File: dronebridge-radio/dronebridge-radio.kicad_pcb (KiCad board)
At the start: 2 copper layers, 20.5 x 28.5 mm, 4 parts, among them J1 Conn_01x06_Pin

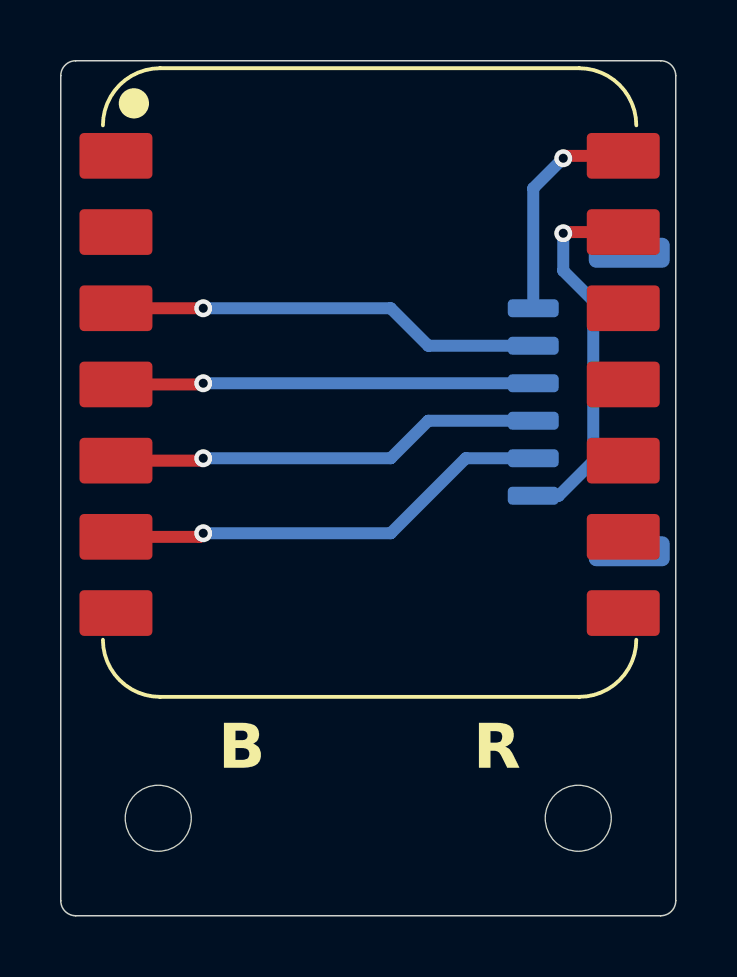
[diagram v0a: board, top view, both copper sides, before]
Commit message: fix swap reset and boot labels on the board
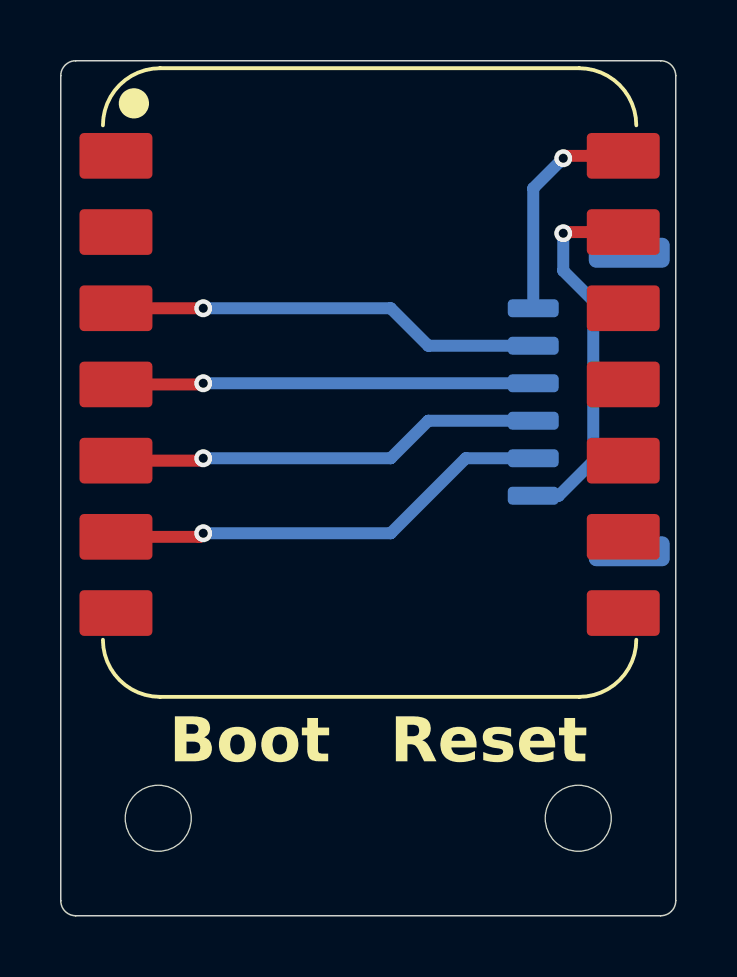
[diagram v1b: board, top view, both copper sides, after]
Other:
- board text added: "Boot"
- board text added: "Reset"
- board text removed: "B"
- board text removed: "R"
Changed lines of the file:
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@@
 (kicad_pcb
-	(version 20240108)
+	(version 20241229)
 	(generator "pcbnew")
-	(generator_version "8.0")
+	(generator_version "9.0")
 	(general
 		(thickness 1.6)
@@
 	(layers
 		(0 "F.Cu" signal)
-		(31 "B.Cu" signal)
-		(32 "B.Adhes" user "B.Adhesive")
-		(33 "F.Adhes" user "F.Adhesive")
-		(34 "B.Paste" user)
-		(35 "F.Paste" user)
-		(36 "B.SilkS" user "B.Silkscreen")
-		(37 "F.SilkS" user "F.Silkscreen")
-		(38 "B.Mask" user)
-		(39 "F.Mask" user)
-		(40 "Dwgs.User" user "User.Drawings")
-		(41 "Cmts.User" user "User.Comments")
-		(42 "Eco1.User" user "User.Eco1")
-		(43 "Eco2.User" user "User.Eco2")
-		(44 "Edge.Cuts" user)
-		(45 "Margin" user)
-		(46 "B.CrtYd" user "B.Courtyard")
-		(47 "F.CrtYd" user "F.Courtyard")
-		(48 "B.Fab" user)
-		(49 "F.Fab" user)
-		(50 "User.1" user)
-		(51 "User.2" user)
-		(52 "User.3" user)
-		(53 "User.4" user)
-		(54 "User.5" user)
-		(55 "User.6" user)
-		(56 "User.7" user)
-		(57 "User.8" user)
-		(58 "User.9" user)
+		(2 "B.Cu" signal)
+		(9 "F.Adhes" user "F.Adhesive")
+		(11 "B.Adhes" user "B.Adhesive")
+		(13 "F.Paste" user)
+		(15 "B.Paste" user)
+		(5 "F.SilkS" user "F.Silkscreen")
+		(7 "B.SilkS" user "B.Silkscreen")
+		(1 "F.Mask" user)
+		(3 "B.Mask" user)
+		(17 "Dwgs.User" user "User.Drawings")
+		(19 "Cmts.User" user "User.Comments")
+		(21 "Eco1.User" user "User.Eco1")
+		(23 "Eco2.User" user "User.Eco2")
+		(25 "Edge.Cuts" user)
+		(27 "Margin" user)
+		(31 "F.CrtYd" user "F.Courtyard")
+		(29 "B.CrtYd" user "B.Courtyard")
+		(35 "F.Fab" user)
+		(33 "B.Fab" user)
+		(39 "User.1" user)
+		(41 "User.2" user)
+		(43 "User.3" user)
+		(45 "User.4" user)
+		(47 "User.5" user)
+		(49 "User.6" user)
+		(51 "User.7" user)
+		(53 "User.8" user)
+		(55 "User.9" user)
 	)
 	(setup
@@
 		(pad_to_mask_clearance 0)
 		(allow_soldermask_bridges_in_footprints no)
+		(tenting front back)
 		(pcbplotparams
-			(layerselection 0x00010fc_ffffffff)
-			(plot_on_all_layers_selection 0x0000000_00000000)
+			(layerselection 0x00000000_00000000_55555555_5755f5ff)
+			(plot_on_all_layers_selection 0x00000000_00000000_00000000_00000000)
 			(disableapertmacros no)
 			(usegerberextensions no)
@@
 			(svgprecision 4)
 			(plotframeref no)
-			(viasonmask no)
 			(mode 1)
 			(useauxorigin no)
@@
 			(pdf_front_fp_property_popups yes)
 			(pdf_back_fp_property_popups yes)
+			(pdf_metadata yes)
+			(pdf_single_document no)
 			(dxfpolygonmode yes)
 			(dxfimperialunits yes)
@@
 			(psnegative no)
 			(psa4output no)
-			(plotreference yes)
-			(plotvalue yes)
-			(plotfptext yes)
-			(plotinvisibletext no)
+			(plot_black_and_white yes)
 			(sketchpadsonfab no)
+			(plotpadnumbers no)
+			(hidednponfab no)
+			(sketchdnponfab yes)
+			(crossoutdnponfab yes)
 			(subtractmaskfromsilk no)
 			(outputformat 1)
@@
 			)
 		)
-		(property "Footprint" "XIAO-ESP32C3-footprints:XIAO-ESP32C3-DIP"
-			(at -0.12 0 90)
-			(unlocked yes)
-			(layer "F.Fab")
-			(hide yes)
-			(effects
-				(font
-					(size 1.27 1.27)
-					(thickness 0.15)
-				)
-			)
-		)
 		(property "Datasheet" ""
 			(at -0.12 0 90)
@@
 				(type solid)
 			)
-			(fill solid)
+			(fill yes)
 			(layer "F.SilkS")
 		)
@@
 				(type default)
 			)
-			(fill none)
+			(fill no)
 			(layer "F.CrtYd")
 		)
@@
 				(type default)
 			)
-			(fill none)
+			(fill no)
 			(layer "F.Fab")
 		)
@@
 				(type solid)
 			)
-			(fill solid)
+			(fill yes)
 			(layer "F.Fab")
 		)
@@
 			(thermal_bridge_angle 45)
 		)
+		(embedded_fonts no)
 		(model "${KIPRJMOD}/XIAO-ESP32C3-footprints/3dmodels/AMz3D.3dshapes/Seeed Studio XIAO-ESP32-C3.step"
 			(offset
@@
 			)
 		)
-		(property "Footprint" "MountingHole:MountingHole_2.2mm_M2"
-			(at 0 0 0)
-			(unlocked yes)
-			(layer "F.Fab")
-			(hide yes)
-			(effects
-				(font
-					(size 1.27 1.27)
-					(thickness 0.15)
-				)
-			)
-		)
 		(property "Datasheet" ""
 			(at 0 0 0)
@@
 				(type solid)
 			)
-			(fill none)
+			(fill no)
 			(layer "Cmts.User")
 		)
@@
 				(type solid)
 			)
-			(fill none)
+			(fill no)
 			(layer "F.CrtYd")
 		)
@@
 			(layers "*.Cu" "*.Mask")
 		)
+		(embedded_fonts no)
 	)
 	(footprint "MountingHole:MountingHole_2.2mm_M2"
@@
 			)
 		)
-		(property "Footprint" "MountingHole:MountingHole_2.2mm_M2"
-			(at 0 0 0)
-			(unlocked yes)
-			(layer "F.Fab")
-			(hide yes)
-			(effects
-				(font
-					(size 1.27 1.27)
-					(thickness 0.15)
-				)
-			)
-		)
 		(property "Datasheet" ""
 			(at 0 0 0)
@@
 				(type solid)
 			)
-			(fill none)
+			(fill no)
 			(layer "Cmts.User")
 		)
@@
 				(type solid)
 			)
-			(fill none)
+			(fill no)
 			(layer "F.CrtYd")
 		)
@@
 			(layers "*.Cu" "*.Mask")
 		)
+		(embedded_fonts no)
 	)
 	(footprint "Connector_JST:JST_GH_SM06B-GHS-TB_1x06-1MP_P1.25mm_Horizontal"
@@
 			)
 		)
-		(property "Footprint" "Connector_JST:JST_GH_SM06B-GHS-TB_1x06-1MP_P1.25mm_Horizontal"
-			(at 0 0 90)
-			(unlocked yes)
-			(layer "B.Fab")
-			(hide yes)
-			(effects
-				(font
-					(size 1.27 1.27)
-					(thickness 0.15)
-				)
-				(justify mirror)
-			)
-		)
 		(property "Datasheet" ""
 			(at 0 0 90)
@@
 			(at -3.125 1.85 270)
 			(size 0.6 1.7)
-			(layers "B.Cu" "B.Paste" "B.Mask")
+			(layers "B.Cu" "B.Mask" "B.Paste")
 			(roundrect_rratio 0.25)
 			(net 12 "+5V")
@@
 			(at -1.875 1.85 270)
 			(size 0.6 1.7)
-			(layers "B.Cu" "B.Paste" "B.Mask")
+			(layers "B.Cu" "B.Mask" "B.Paste")
 			(roundrect_rratio 0.25)
 			(net 13 "/RX")
@@
 			(at -0.625 1.85 270)
 			(size 0.6 1.7)
-			(layers "B.Cu" "B.Paste" "B.Mask")
+			(layers "B.Cu" "B.Mask" "B.Paste")
 			(roundrect_rratio 0.25)
 			(net 3 "/TX")
@@
 			(at 0.625 1.85 270)
 			(size 0.6 1.7)
-			(layers "B.Cu" "B.Paste" "B.Mask")
+			(layers "B.Cu" "B.Mask" "B.Paste")
 			(roundrect_rratio 0.25)
 			(net 6 "/RTS")
@@
 			(at 1.875 1.85 270)
 			(size 0.6 1.7)
-			(layers "B.Cu" "B.Paste" "B.Mask")
+			(layers "B.Cu" "B.Mask" "B.Paste")
 			(roundrect_rratio 0.25)
 			(net 2 "/CTS")
@@
 			(at 3.125 1.85 270)
 			(size 0.6 1.7)
-			(layers "B.Cu" "B.Paste" "B.Mask")
+			(layers "B.Cu" "B.Mask" "B.Paste")
 			(roundrect_rratio 0.25)
 			(net 9 "GND")
@@
 			(at -4.975 -1.35 270)
 			(size 1 2.7)
-			(layers "B.Cu" "B.Paste" "B.Mask")
+			(layers "B.Cu" "B.Mask" "B.Paste")
 			(roundrect_rratio 0.25)
 		)
@@
 			(at 4.975 -1.35 270)
 			(size 1 2.7)
-			(layers "B.Cu" "B.Paste" "B.Mask")
+			(layers "B.Cu" "B.Mask" "B.Paste")
 			(roundrect_rratio 0.25)
 		)
+		(embedded_fonts no)
 		(model "${KICAD8_3DMODEL_DIR}/Connector_JST.3dshapes/JST_GH_SM06B-GHS-TB_1x06-1MP_P1.25mm_Horizontal.wrl"
 			(offset
@@
 			(type solid)
 		)
-		(fill solid)
+		(fill yes)
 		(layer "B.SilkS")
 	)
@@
 		)
 		(layer "Edge.Cuts")
+	)
+	(gr_text "Reset"
+		(at 133.731 97.536 0)
+		(layer "F.SilkS")
+		(effects
+			(font
+				(size 1.5 1.5)
+				(thickness 0.3)
+				(bold yes)
+			)
+			(justify left bottom)
+		)
+	)
+	(gr_text "Boot"
+		(at 126.365 97.536 0)
+		(layer "F.SilkS")
+		(effects
+			(font
+				(size 1.5 1.5)
+				(thickness 0.3)
+				(bold yes)
+			)
+			(justify left bottom)
+		)
 	)
 	(gr_text "5V"
@@
 		)
 	)
-	(gr_text "R"
-		(at 136.5 97.75 0)
-		(layer "F.SilkS")
-		(effects
-			(font
-				(size 1.5 1.5)
-				(thickness 0.3)
-				(bold yes)
-			)
-			(justify left bottom)
-		)
-	)
-	(gr_text "B"
-		(at 128 97.75 0)
-		(layer "F.SilkS")
-		(effects
-			(font
-				(size 1.5 1.5)
-				(thickness 0.3)
-				(bold yes)
-			)
-			(justify left bottom)
-		)
-	)
 	(segment
 		(start 124.59 89.87)
@@
 		(net 13)
 	)
+	(embedded_fonts no)
 )
